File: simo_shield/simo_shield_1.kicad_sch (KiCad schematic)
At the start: 5 parts, among them J1 PORT SWD, U1 YAAJ_BluePill_Part_Like_SWD_B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, U2 elemon_board, U3 flash_externa, U4 mpu6050

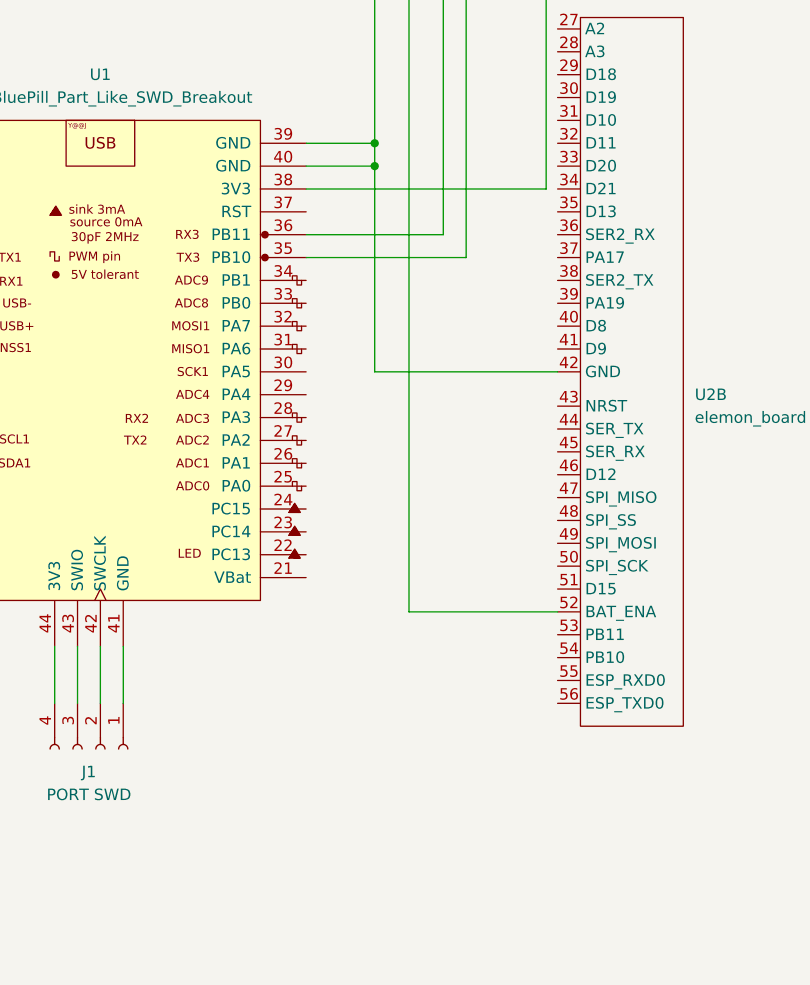
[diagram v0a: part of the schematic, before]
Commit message: se agrego conector de bateria a ambas placas
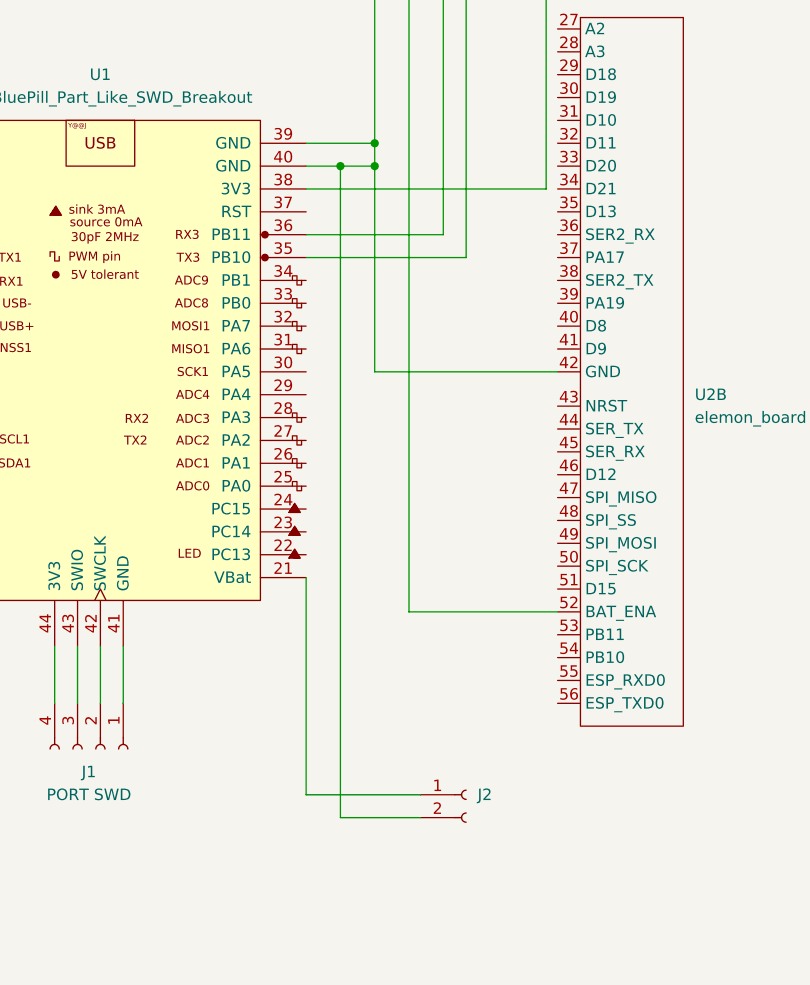
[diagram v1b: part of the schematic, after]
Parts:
- added J2: (no value), symbol Connector:Conn_01x02_Female
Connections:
- net at U1.21 (VBat): now also J2.1 (Pin_1)
- net at U1.39 (GND), U1.40 (GND), U2.42 (GND)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: now also J2.2 (Pin_2)
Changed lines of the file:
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@@
   (junction (at 168.91 62.23) (diameter 0) (color 0 0 0 0)
   )
+  (junction (at 165.1 62.23) (diameter 0) (color 0 0 0 0)
+  )
   (junction (at 97.79 110.49) (diameter 0) (color 0 0 0 0)
   )
@@
     (stroke (width 0) (type default) (color 0 0 0 0))
   )
+  (wire (pts (xy 165.1 134.62) (xy 165.1 62.23))
+    (stroke (width 0) (type default) (color 0 0 0 0))
+  )
   (wire (pts (xy 189.23 85.09) (xy 168.91 85.09))
     (stroke (width 0) (type default) (color 0 0 0 0))
@@
     (stroke (width 0) (type default) (color 0 0 0 0))
   )
+  (wire (pts (xy 173.99 134.62) (xy 165.1 134.62))
+    (stroke (width 0) (type default) (color 0 0 0 0))
+  )
   (wire (pts (xy 97.79 68.58) (xy 87.63 68.58))
     (stroke (width 0) (type default) (color 0 0 0 0))
@@
     (stroke (width 0) (type default) (color 0 0 0 0))
   )
+  (wire (pts (xy 165.1 62.23) (xy 168.91 62.23))
+    (stroke (width 0) (type default) (color 0 0 0 0))
+  )
   (wire (pts (xy 81.28 132.08) (xy 114.3 132.08))
     (stroke (width 0) (type default) (color 0 0 0 0))
@@
     (stroke (width 0) (type default) (color 0 0 0 0))
   )
+  (wire (pts (xy 161.29 132.08) (xy 161.29 107.95))
+    (stroke (width 0) (type default) (color 0 0 0 0))
+  )
   (wire (pts (xy 187.96 35.56) (xy 168.91 35.56))
     (stroke (width 0) (type default) (color 0 0 0 0))
@@
     (stroke (width 0) (type default) (color 0 0 0 0))
   )
-  (wire (pts (xy 161.29 62.23) (xy 168.91 62.23))
+  (wire (pts (xy 161.29 62.23) (xy 165.1 62.23))
     (stroke (width 0) (type default) (color 0 0 0 0))
   )
@@
   )
   (wire (pts (xy 87.63 110.49) (xy 97.79 110.49))
+    (stroke (width 0) (type default) (color 0 0 0 0))
+  )
+  (wire (pts (xy 173.99 132.08) (xy 161.29 132.08))
     (stroke (width 0) (type default) (color 0 0 0 0))
   )
@@
     (pin "56")
   )
+  (symbol (lib_id "Connector:Conn_01x02_Female") (at 179.07 132.08 0) (unit 1)
+    (in_bom yes) (on_board yes) (fields_autoplaced)
+    (property "Reference" "J2" (id 0) (at 180.34 132.0799 0)
+      (effects (font (size 1.27 1.27)) (justify left))
+    )
+    (property "Value" "" (id 1) (at 180.34 134.6199 0)
+      (effects (font (size 1.27 1.27)) (justify left))
+    )
+    (property "Footprint" "" (id 2) (at 179.07 132.08 0)
+      (effects (font (size 1.27 1.27)) hide)
+    )
+    (property "Datasheet" "~" (id 3) (at 179.07 132.08 0)
+      (effects (font (size 1.27 1.27)) hide)
+    )
+    (pin "1")
+    (pin "2")
+  )
   (symbol (lib_name "elemon_board_1") (lib_id "simo_board:elemon_board") (at 85.09 43.18 0) (mirror y) (unit 1)
     (in_bom yes) (on_board yes)
@@
       (reference "J1") (unit 1) (value "PORT SWD") (footprint "Connector_PinHeader_2.54mm:PinHeader_1x04_P2.54mm_Vertical")
     )
+    (path "/3a2b4e4a-e4df-4836-8ba6-f50f59704c20"
+      (reference "J2") (unit 1) (value "VBAT") (footprint "Connector_JST:JST_EH_B2B-EH-A_1x02_P2.50mm_Vertical")
+    )
     (path "/13088b32-4e75-4353-a23a-47b0cf7f1d07"

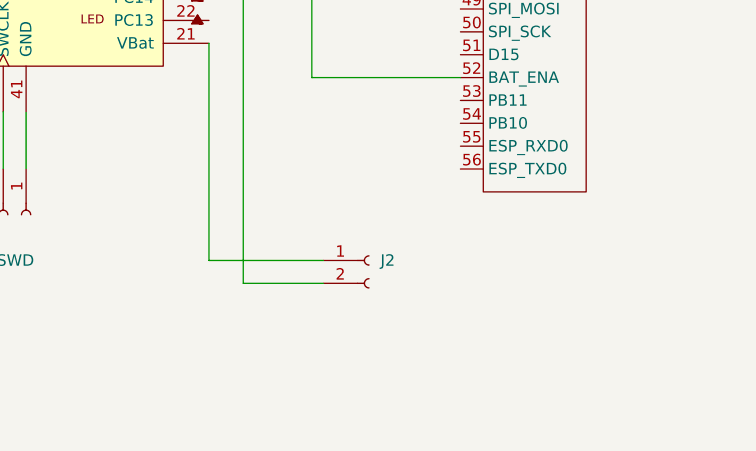
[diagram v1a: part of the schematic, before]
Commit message: se guardaron modelos 3d de ambas placas en formato step
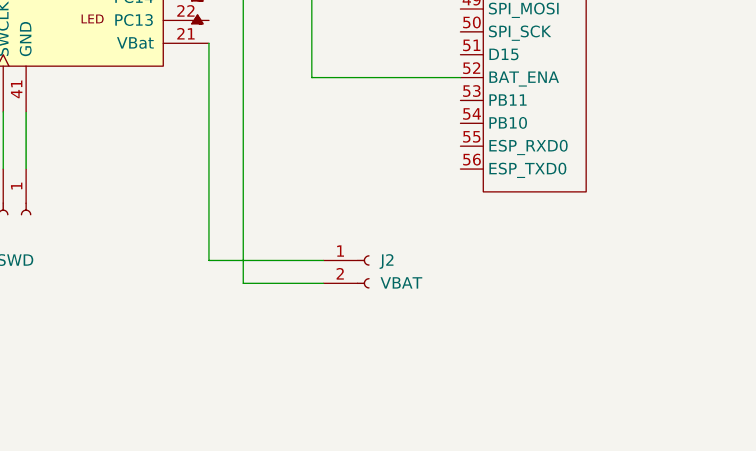
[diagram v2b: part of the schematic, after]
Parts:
- J2: value (none) -> VBAT; footprint (none) -> Connector_JST:JST_EH_B2B-EH-A_1x02_P2.50mm_Vertical
- U2: footprint elemon:elemon_board -> (none)
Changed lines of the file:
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@@
       (effects (font (size 1.27 1.27)) (justify left))
     )
-    (property "Footprint" "elemon:elemon_board" (id 2) (at 191.77 44.45 0)
+    (property "Footprint" "" (id 2) (at 191.77 44.45 0)
       (effects (font (size 1.27 1.27)) hide)
     )
@@
       (effects (font (size 1.27 1.27)) (justify left))
     )
-    (property "Value" "" (id 1) (at 180.34 134.6199 0)
-      (effects (font (size 1.27 1.27)) (justify left))
-    )
-    (property "Footprint" "" (id 2) (at 179.07 132.08 0)
+    (property "Value" "VBAT" (id 1) (at 180.34 134.6199 0)
+      (effects (font (size 1.27 1.27)) (justify left))
+    )
+    (property "Footprint" "Connector_JST:JST_EH_B2B-EH-A_1x02_P2.50mm_Vertical" (id 2) (at 179.07 132.08 0)
       (effects (font (size 1.27 1.27)) hide)
     )
@@
       (effects (font (size 1.27 1.27)) (justify left))
     )
-    (property "Footprint" "elemon:elemon_board" (id 2) (at 85.09 43.18 0)
+    (property "Footprint" "" (id 2) (at 85.09 43.18 0)
       (effects (font (size 1.27 1.27)) hide)
     )
@@
     )
     (path "/67356e78-0efe-482f-a454-ed1826d52ea6"
-      (reference "U2") (unit 1) (value "elemon_board") (footprint "elemon:elemon_board")
+      (reference "U2") (unit 1) (value "elemon_board") (footprint "elemon_board:elemon_board")
     )
     (path "/1e823c03-b937-4ab7-abb4-e3fa1b077214"
-      (reference "U2") (unit 2) (value "elemon_board") (footprint "elemon:elemon_board")
+      (reference "U2") (unit 2) (value "elemon_board") (footprint "elemon_board:elemon_board")
     )
     (path "/92407edf-e640-450c-9281-41ac46831b00"

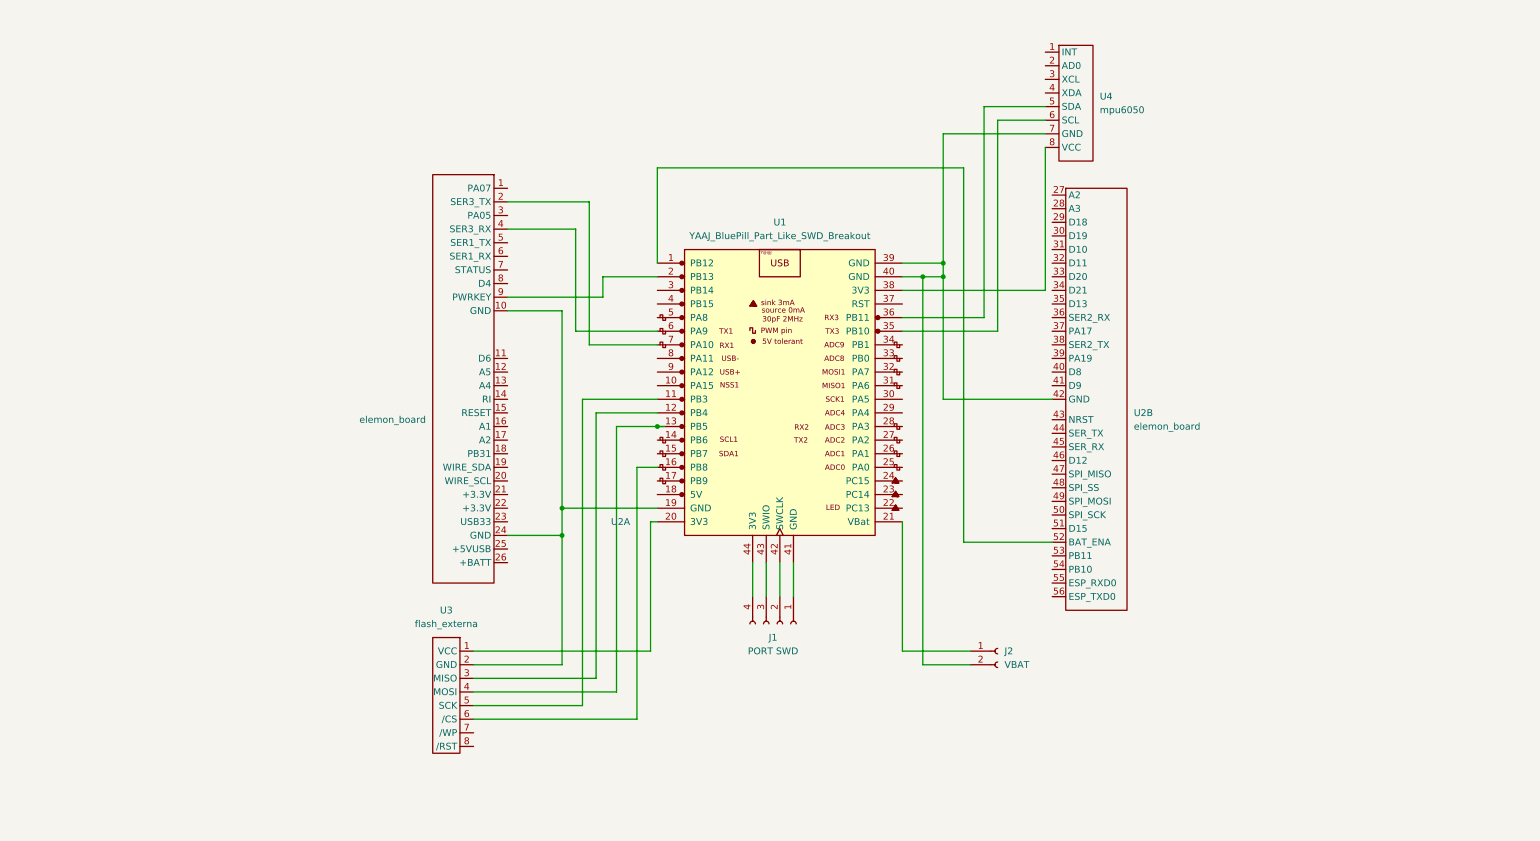
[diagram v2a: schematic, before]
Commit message: se diseñaron las pistas de placa shield simo, revisar
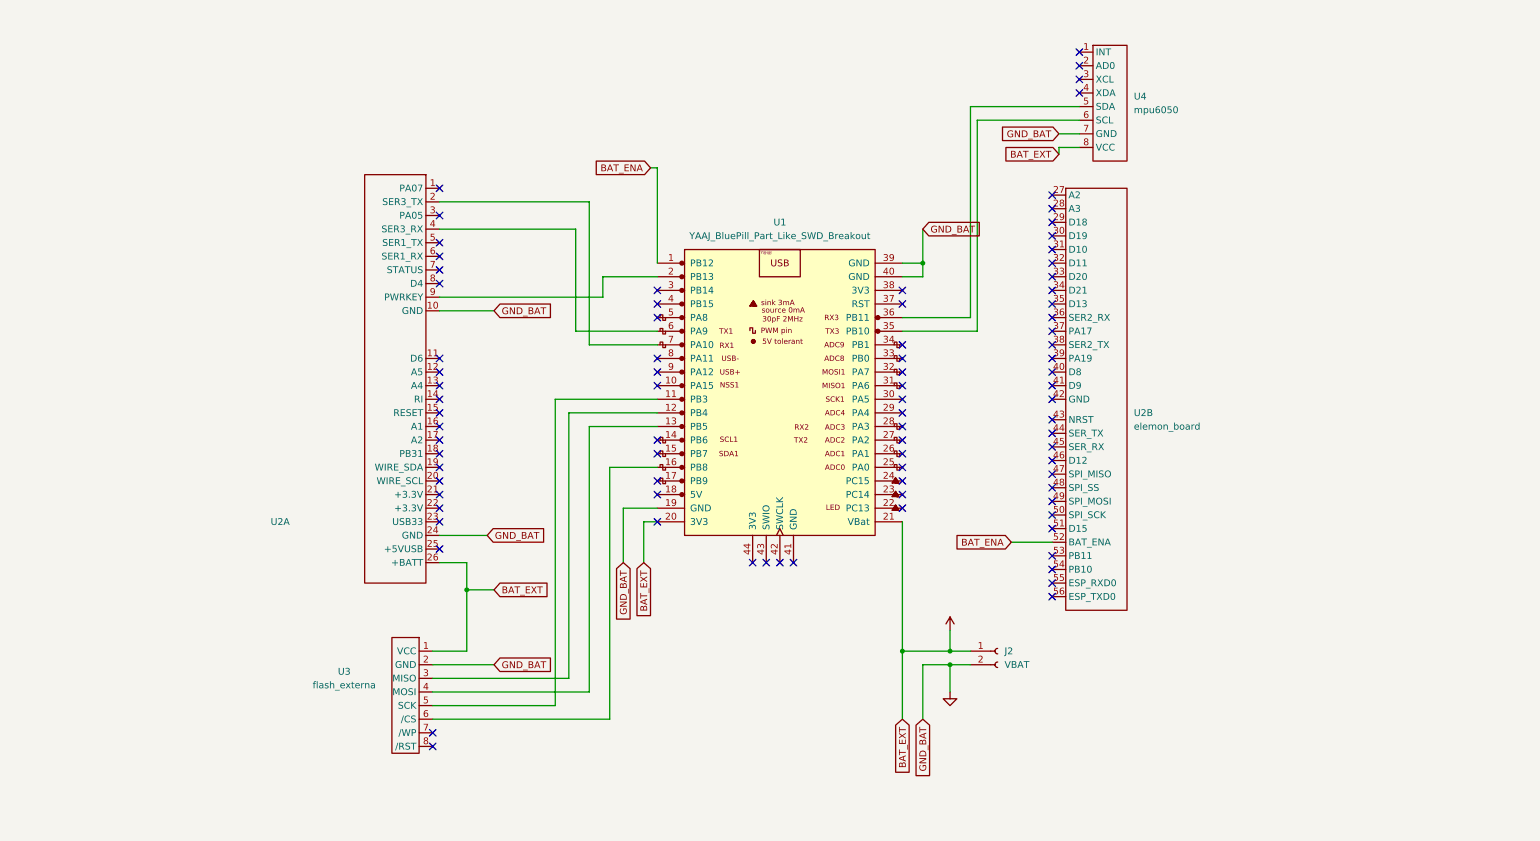
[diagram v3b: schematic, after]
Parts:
- removed J1: PORT SWD, Connector_PinHeader_2.54mm:PinHeader_1x04_P2.54mm_Vertical, symbol Connector:Conn_01x04_Female
- U2: footprint (none) -> elemon_board:elemon_board
- U2: value elemon_board -> (none)
- U4: footprint mpu6050:MPU6050 -> (none)
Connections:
- net BAT_ENA: now reaches U1.1 (PB12), U2.52 (BAT_ENA)
- net GND: now reaches U1.19 (GND), U2.10 (GND), U2.24 (GND), U3.2 (GND)
- net GND: now also J2.2 (Pin_2), U1.39 (GND), U1.40 (GND), U4.7 (GND)
- net +BATT: now reaches U1.20 (3V3), U3.1 (VCC)
- net +BATT: now also J2.1 (Pin_1), U1.21 (VBat), U2.26 (+BATT), U4.8 (VCC)
- net at U1.38 (3V3): no longer U4.8 (VCC)
- now unconnected: U2.42 (GND)
- no-connect marks 0 -> 85
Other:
- moved on the sheet: U2A, U3, U4

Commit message: verifique conexiones en simo shield, todo ok.
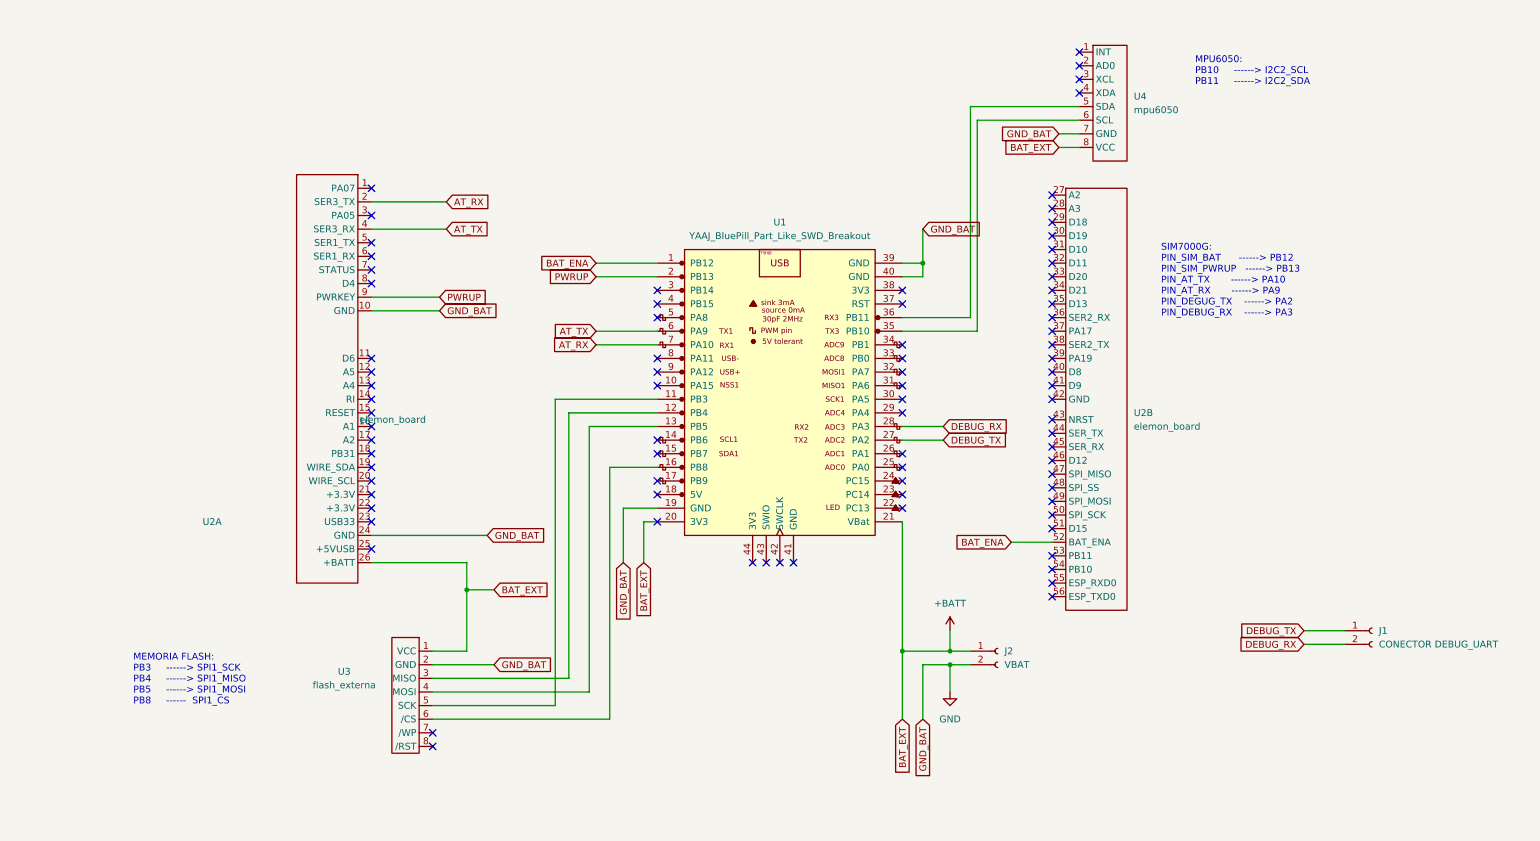
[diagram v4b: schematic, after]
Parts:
- added J1: CONECTOR DEBUG_UART, Connector_JST:JST_EH_B2B-EH-A_1x02_P2.50mm_Vertical, symbol Connector:Conn_01x02_Female
- U2: value (none) -> elemon_board; footprint (none) -> elemon_board:elemon_board
- U4: footprint (none) -> simo_mpu6050:MPU6050
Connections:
- net PWRUP: now reaches U1.2 (PB13), U2.9 (PWRKEY)
- net DEBUG_TX: now reaches U1.27 (PA2)
- net DEBUG_TX: now also J1.1 (Pin_1)
- net DEBUG_RX: now reaches U1.28 (PA3)
- net DEBUG_RX: now also J1.2 (Pin_2)
- net AT_TX: now reaches U1.6 (PA9), U2.4 (SER3_RX)
- net AT_RX: now reaches U1.7 (PA10), U2.2 (SER3_TX)
- no-connect marks 85 -> 83
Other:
- note added: "MEMORIA FLASH: PB3 ------> SPI1_SCK PB4 ------> SPI1_MISO PB5 ------> SPI1_MOSI PB8 ------ SPI1_CS"
- note added: "MPU6050: PB10 ------> I2C2_SCL PB11 ------> I2C2_SDA"
- note added: "SIM7000G: PIN_SIM_BAT ------> PB12 PIN_SIM_PWRUP ------> PB13 PIN_AT_TX ------> PA10 PIN_AT_RX ------> PA9 PIN_DEGUG_TX ------> PA2 PIN_DEBUG_RX ------> PA3"
- moved on the sheet: U2A
